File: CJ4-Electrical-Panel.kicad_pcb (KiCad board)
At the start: 2 copper layers, 122.4 x 62.5 mm, 43 parts, among them J1 Conn_01x03, J2 Conn_01x03, J3 Conn_01x03, J4 Conn_01x03, J5 Conn_01x03, J6 Conn_01x03, J7 USB_B_Mini, J8 AVR-ISP-6, U1 ATmega32U4-A, Y1 16MHz

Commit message: All routed and ready for fab
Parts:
- J1, J2, J3, J4, J5, J6: footprint Connector_JST:JST_XH_B3B-XH-AM_1x03_P2.50mm_Vertical -> Connector_JST:JST_XH_B3B-XH-A_1x03_P2.50mm_Vertical
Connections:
- U1 pad 31: unconnected-(U1-Pad31) -> LGEN_RESET
- U1 pad 32: unconnected-(U1-Pad32) -> LGEN_ON
- U1 pad 36: LGEN_RESET -> EMERLT_ON
- U1 pad 37: LGEN_ON -> EMERLT_ARMED
- U1 pad 38: EMERLT_ON -> BATTERY_EMER
- U1 pad 39: EMERLT_ARMED -> BATTERY_ON
- U1 pad 40: BATTERY_EMER -> unconnected-(U1-Pad40)
- U1 pad 41: BATTERY_ON -> unconnected-(U1-Pad41)
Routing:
- net LGEN_RESET: track 67.6 -> 83.3 mm
- net LGEN_ON: track 65.5 -> 78.3 mm
- net +5V: track 72.3 -> 82.2 mm
- net RESET: track 20.7 -> 22.2 mm, vias 0 -> 2
- net /VBUS: track 1.79 -> 2.83 mm
- net BATTERY_EMER: track 15.2 -> 15.8 mm
- net BATTERY_ON: track 12.3 -> 13.0 mm
- net EMERLT_ARMED: track 38.4 -> 39.1 mm
- removed copper zone on B.Cu, net /VBUS
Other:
- board text added: "@version@"
- board text added: "CJ4 electrical panel Neil Enns neile@live.com @date@ @version@"
- board text added: "JLCJLCJLCJLC"
- board text removed: "CJ4 electrical panel Neil Enns neile@live.com @date@ @version@ JLCJLCJLCJLC"
- board text removed: "STBY FLT DISPLAY ON"

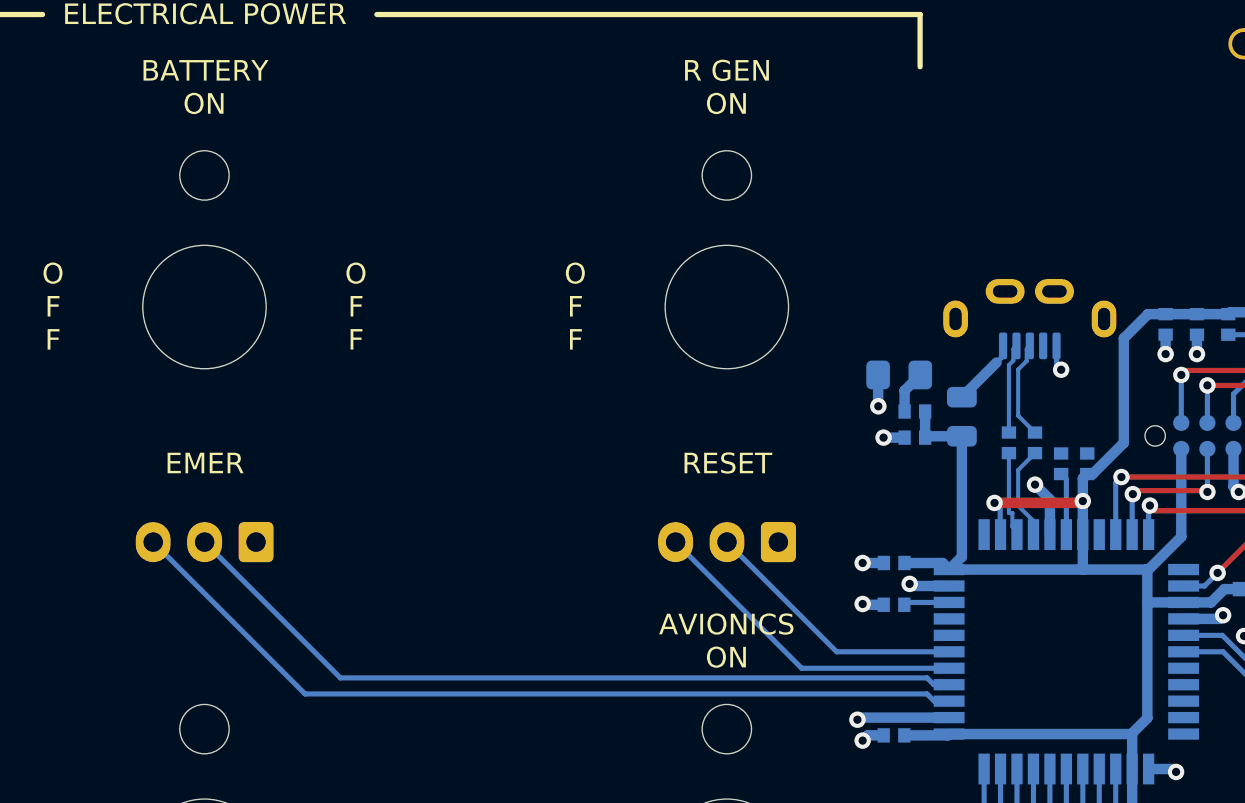
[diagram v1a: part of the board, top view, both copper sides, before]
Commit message: Change USB connector, add missing labels
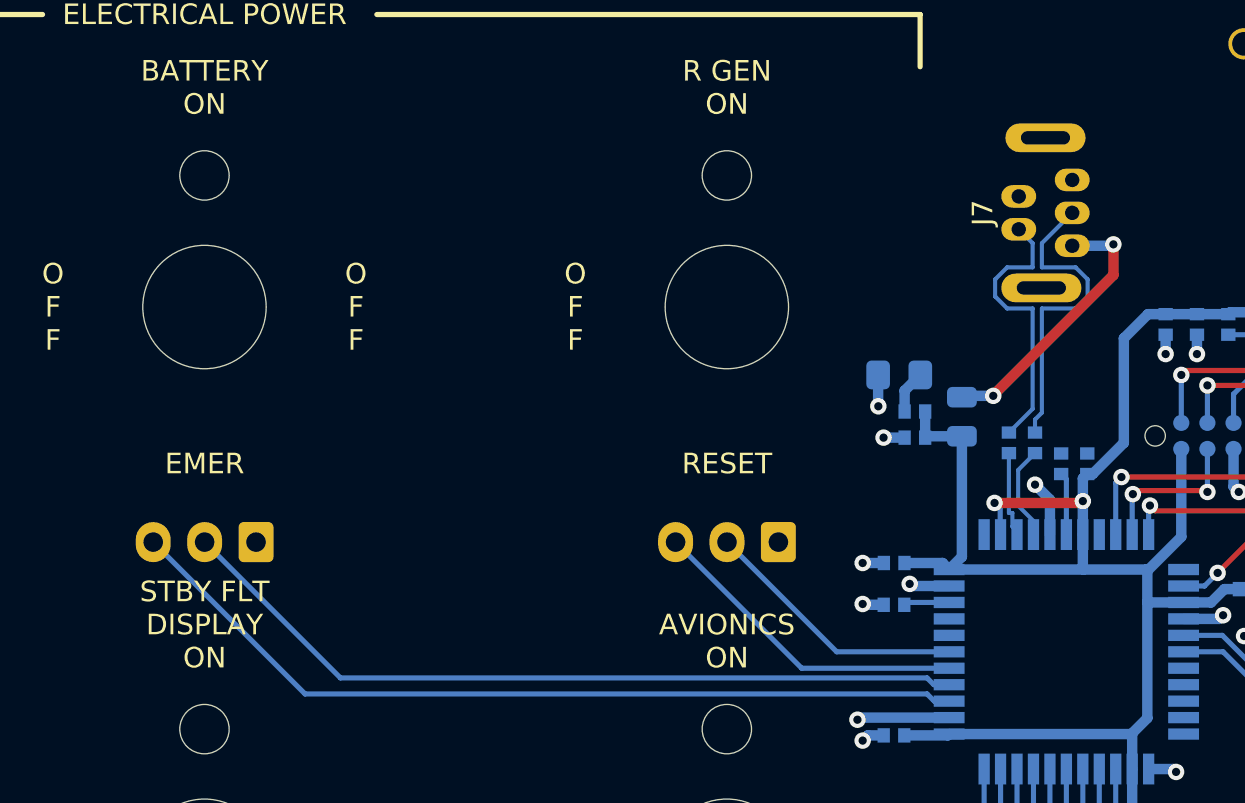
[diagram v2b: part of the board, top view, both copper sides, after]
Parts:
- J7: value USB_B_Mini -> USB_B_Micro; footprint CJ4-Electrical-Panel:ZX80-B-5P -> CJ4-Electrical-Panel:USB_B_Mini_Amphenol_UE25BE5510H; moved to F.Cu
- moved J7 5.14 mm to (152.9, 64.0), turned to -90 degrees
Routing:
- net /VBUS: track 2.83 -> 13.4 mm, vias 0 -> 2
- net /DR+: track 4.79 -> 15.2 mm
- net /DR-: track 4.35 -> 13.6 mm
- net GND: track 31.6 -> 30.4 mm, vias 21 -> 20
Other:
- board text added: "STBY FLT DISPLAY ON"

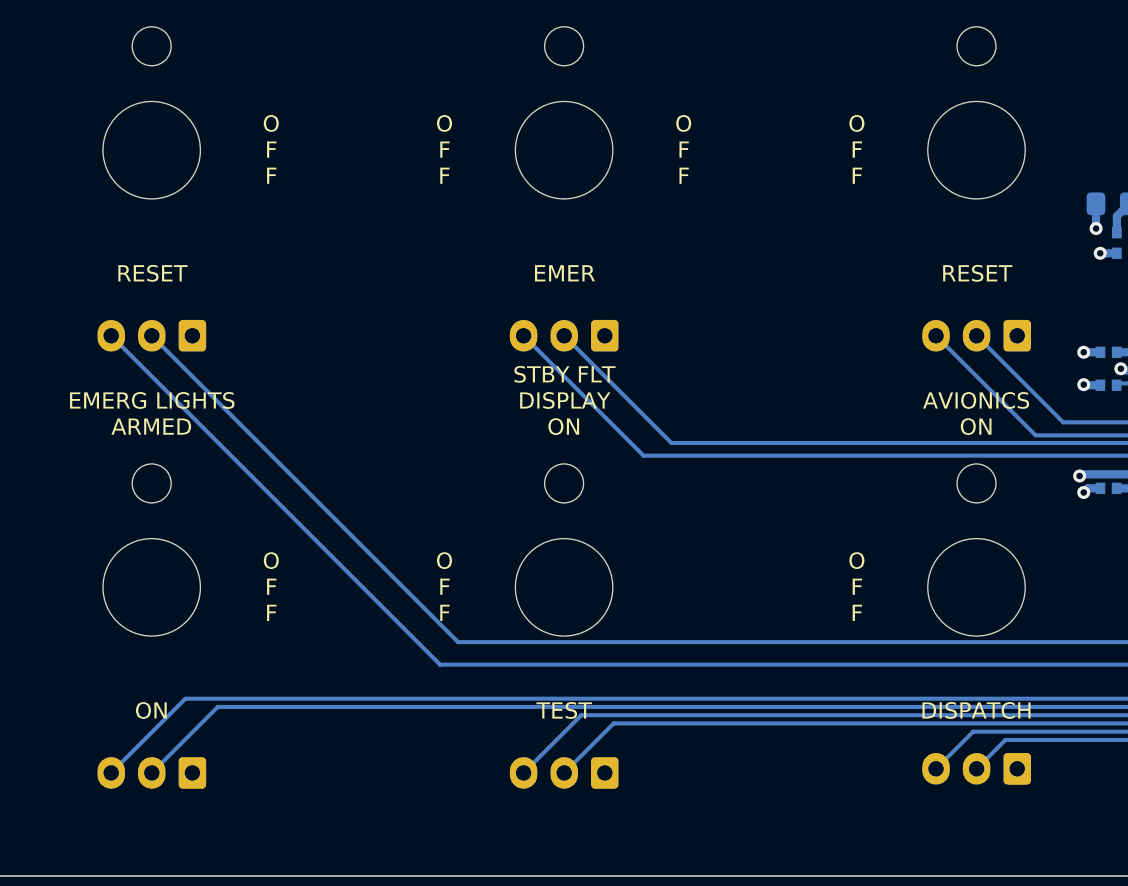
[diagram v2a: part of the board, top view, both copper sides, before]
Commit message: Fixes Make switch holes bigger #2
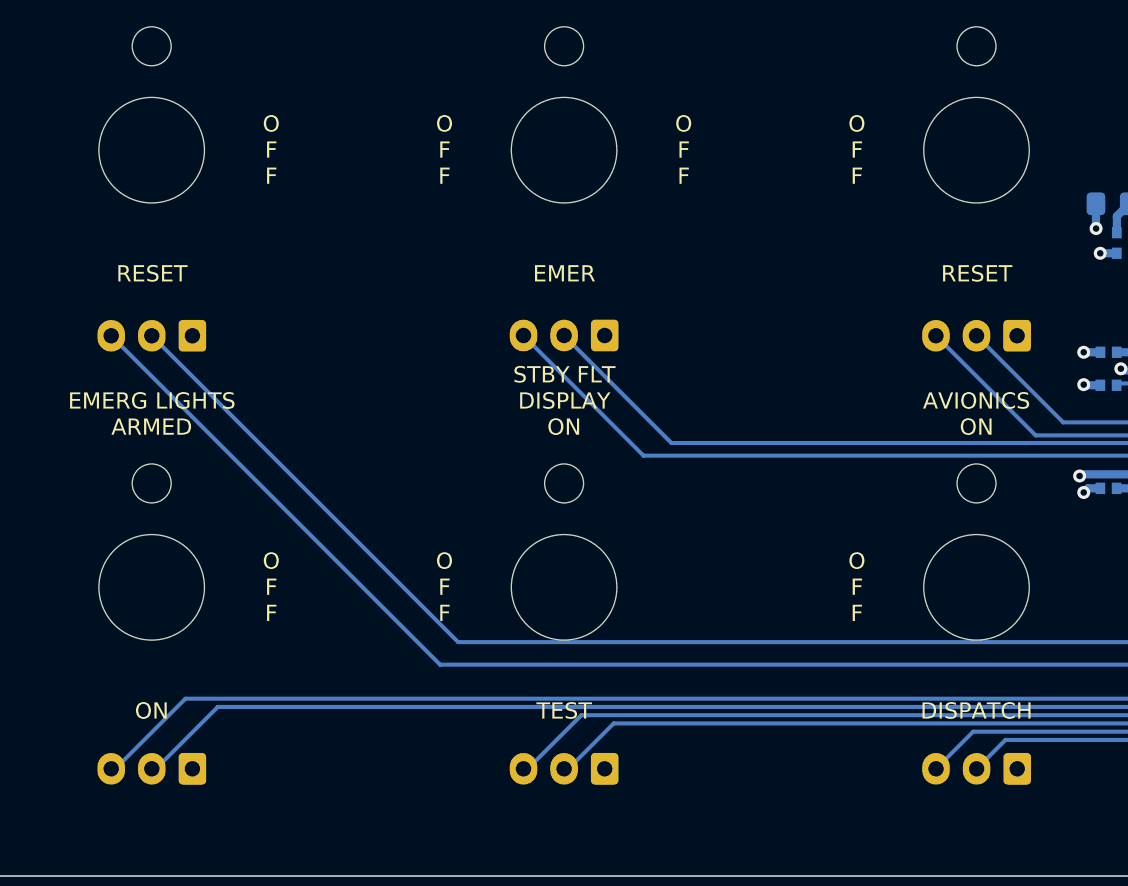
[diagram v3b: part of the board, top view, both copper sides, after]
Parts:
- moved J5 37.0 mm to (139.9, 80.0)
- moved J2 36.8 mm to (89.1, 106.7)
- moved J3 25.4 mm to (114.5, 80.0)
- moved J4 25.4 mm to (114.5, 106.7)
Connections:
- U1 pad 27: RGEN_ON -> STBY_ON
- U1 pad 28: RGEN_RESET -> STBY_TEST
- U1 pad 29: STBY_ON -> EMERLT_ARMED
- U1 pad 30: STBY_TEST -> EMERLT_ON
- U1 pad 36: EMERLT_ON -> BATTERY_EMER
- U1 pad 37: EMERLT_ARMED -> BATTERY_ON
- U1 pad 38: BATTERY_EMER -> RGEN_RESET
- U1 pad 39: BATTERY_ON -> RGEN_ON
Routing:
- net RGEN_ON: track 54.4 -> 13.0 mm
- net RGEN_RESET: track 55.8 -> 15.8 mm
- net EMERLT_ARMED: track 39.1 -> 77.5 mm
- net EMERLT_ON: track 41.9 -> 78.8 mm
- net BATTERY_ON: track 13.0 -> 39.1 mm
- net BATTERY_EMER: track 15.8 -> 41.9 mm
- net STBY_ON: track 77.5 -> 54.4 mm
- net STBY_TEST: track 78.8 -> 55.8 mm

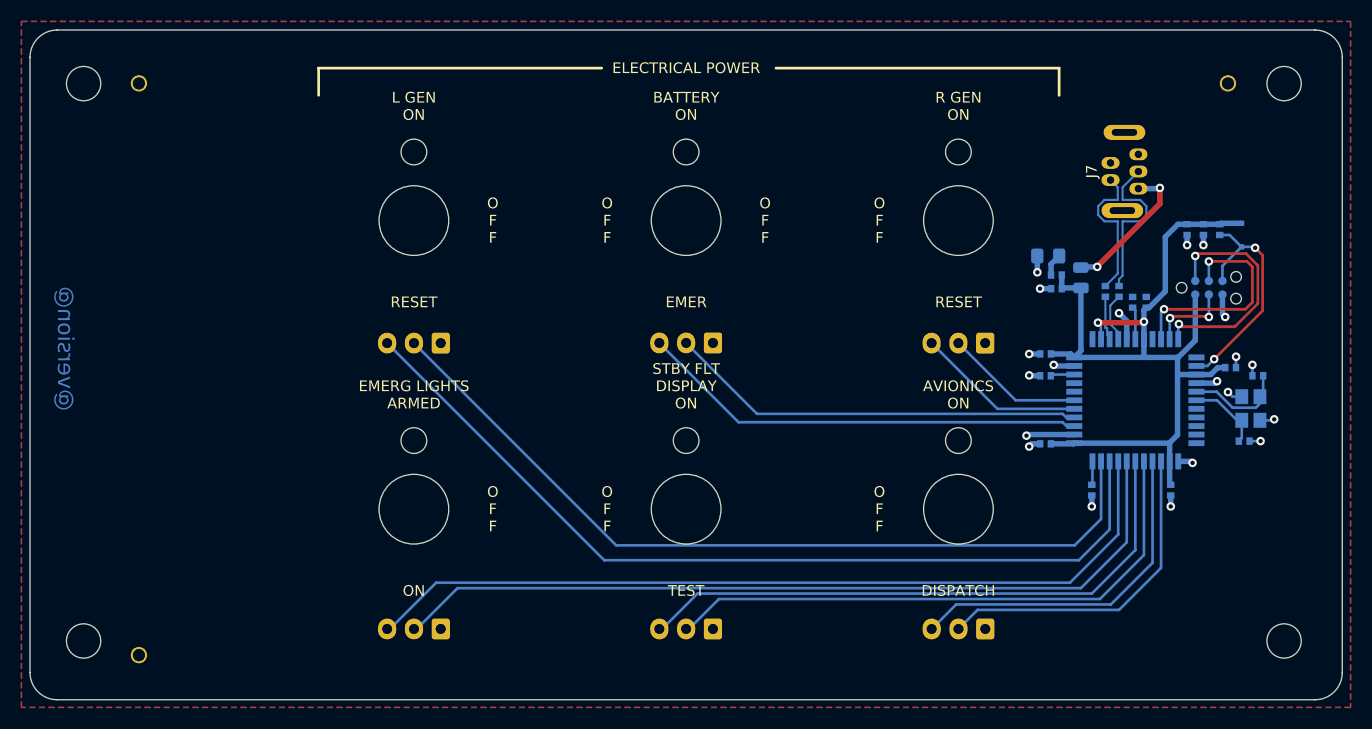
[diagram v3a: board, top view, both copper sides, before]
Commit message: Replace USB connector Fixes #1
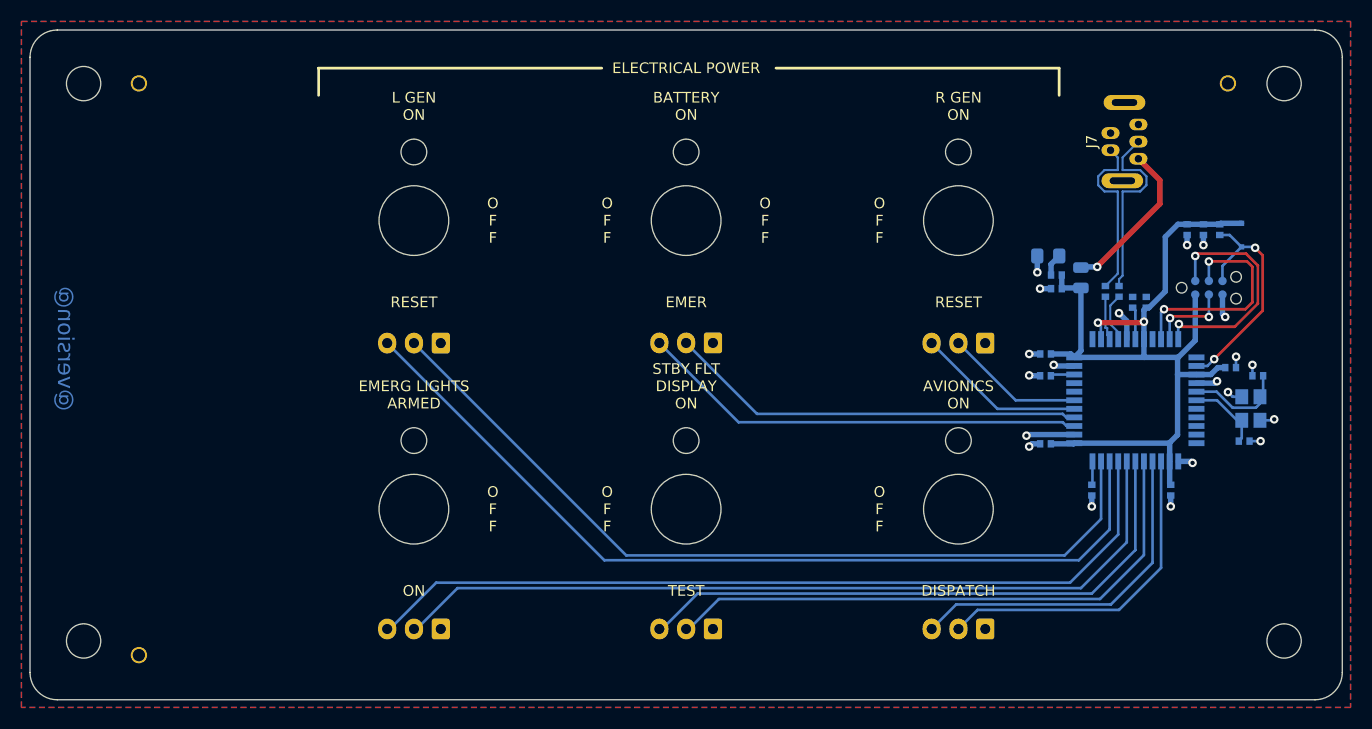
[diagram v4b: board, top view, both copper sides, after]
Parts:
- J7: value USB_B_Micro -> USB_B_Mini
- moved J7 2.79 mm to (152.9, 61.2)
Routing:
- net /DR+: track 15.2 -> 18.0 mm
- net /DR-: track 13.6 -> 16.4 mm
- net /VBUS: track 13.4 -> 14.9 mm, vias 2 -> 1
- net LGEN_ON: track 78.3 -> 79.1 mm
